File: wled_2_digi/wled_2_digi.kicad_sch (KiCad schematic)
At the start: 31 parts, among them J1 Barrel_Jack_Switch, J3 Screw_Terminal_01x04, J4 Screw_Terminal_01x04, Q2 AP15P04S, Q3 MMBT2222A, Q4 MMBT2222A, Q5 AP15P04S, U1 74AHCT125, U2 AP63205WU, U3 Screw Terminal

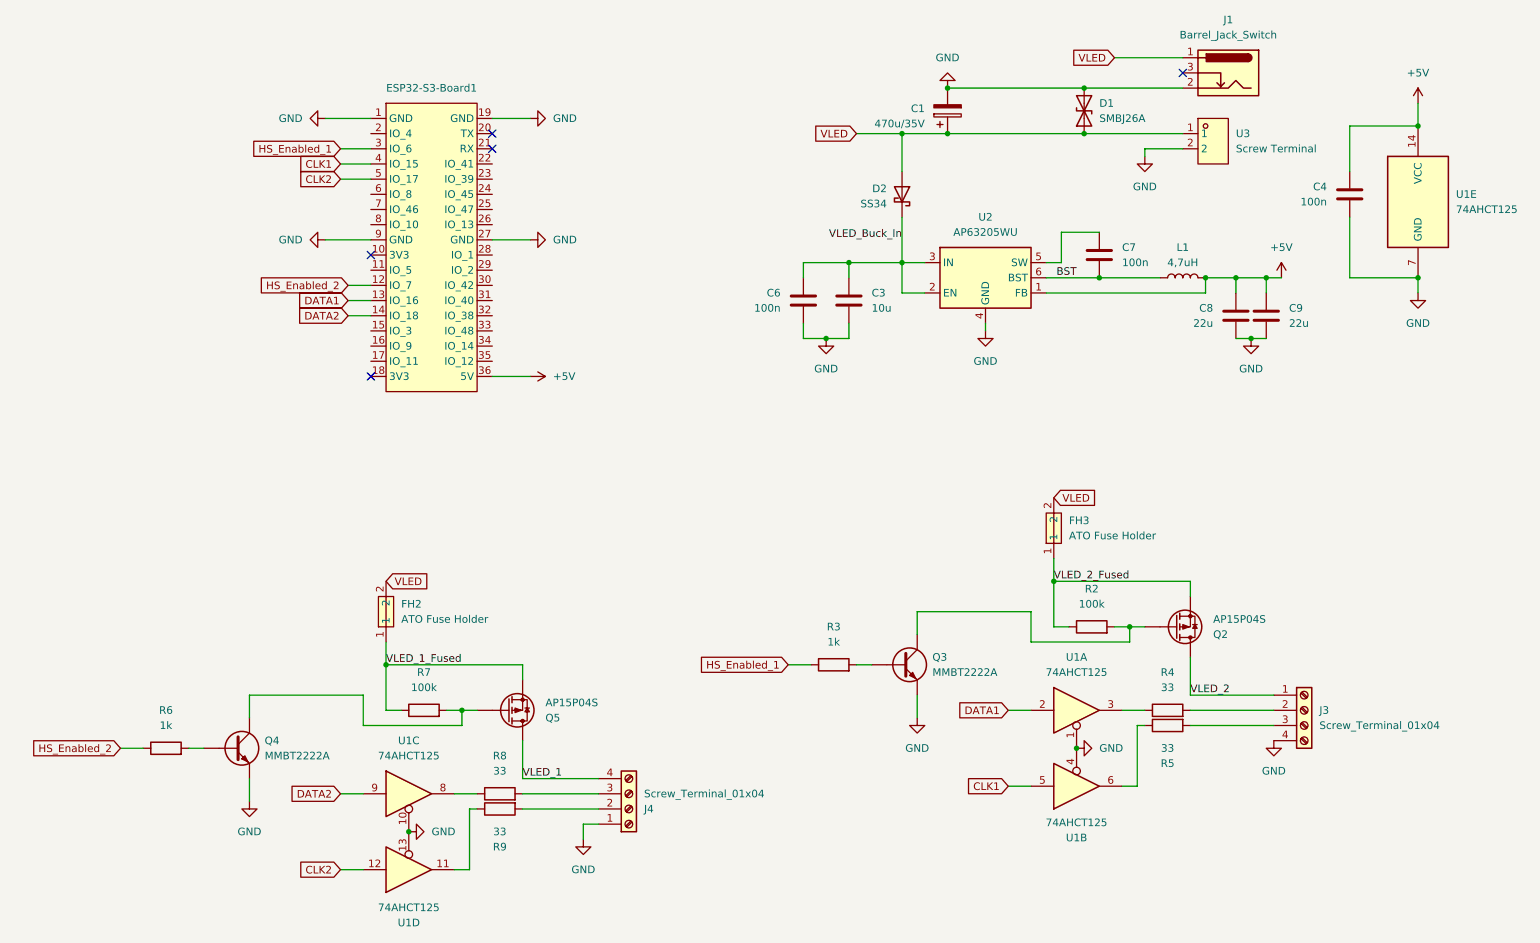
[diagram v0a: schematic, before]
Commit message: Moved components closer
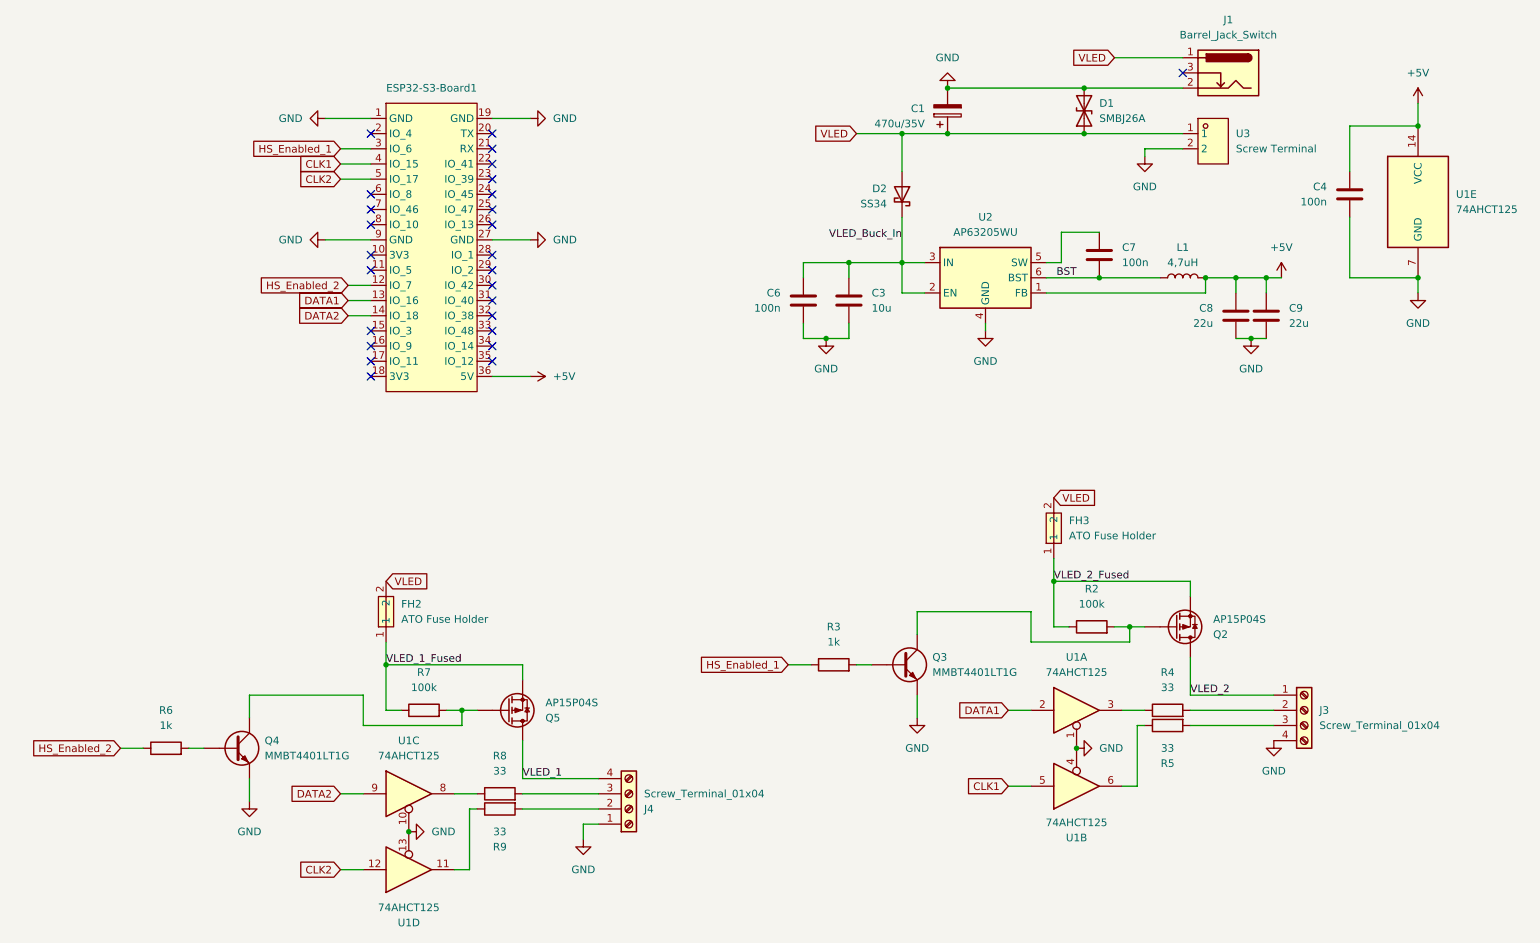
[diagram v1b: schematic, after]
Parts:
- Q3, Q4: value MMBT2222A -> MMBT4401LT1G
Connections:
- no-connect marks 5 -> 26
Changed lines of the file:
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@@
 	)
 	(no_connect
+		(at 99.06 55.88)
+	)
+	(no_connect
 		(at 78.74 83.82)
 	)
 	(no_connect
+		(at 78.74 53.34)
+	)
+	(no_connect
+		(at 99.06 68.58)
+	)
+	(no_connect
+		(at 78.74 55.88)
+	)
+	(no_connect
+		(at 78.74 66.04)
+	)
+	(no_connect
+		(at 99.06 81.28)
+	)
+	(no_connect
+		(at 78.74 78.74)
+	)
+	(no_connect
 		(at 99.06 45.72)
 	)
 	(no_connect
+		(at 99.06 71.12)
+	)
+	(no_connect
+		(at 99.06 58.42)
+	)
+	(no_connect
+		(at 78.74 43.18)
+	)
+	(no_connect
+		(at 78.74 76.2)
+	)
+	(no_connect
+		(at 78.74 81.28)
+	)
+	(no_connect
+		(at 78.74 58.42)
+	)
+	(no_connect
+		(at 99.06 48.26)
+	)
+	(no_connect
+		(at 99.06 78.74)
+	)
+	(no_connect
+		(at 99.06 76.2)
+	)
+	(no_connect
+		(at 99.06 66.04)
+	)
+	(no_connect
 		(at 78.74 63.5)
 	)
 	(no_connect
+		(at 99.06 50.8)
+	)
+	(no_connect
+		(at 99.06 53.34)
+	)
+	(no_connect
+		(at 99.06 63.5)
+	)
+	(no_connect
+		(at 99.06 73.66)
+	)
+	(no_connect
 		(at 99.06 43.18)
 	)
@@
 			)
 		)
-		(property "Value" "MMBT2222A"
+		(property "Value" "MMBT4401LT1G"
 			(at 60.96 147.3199 0)
 			(show_name no)
@@
 			)
 		)
-		(property "Value" "MMBT2222A"
+		(property "Value" "MMBT4401LT1G"
 			(at 172.72 133.3499 0)
 			(show_name no)
